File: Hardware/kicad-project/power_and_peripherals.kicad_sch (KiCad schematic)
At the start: 42 parts, among them CN1 Conn_02x08_Odd_Even, CN2 Conn_02x15_Odd_Even, CN3 Conn_02x17_Odd_Even, CN4 Conn_02x10_Odd_Even, J1 Conn_01x02, J2 UART, J3 Torque, J4 Stepper supply, J5 Brake, Q1 Q_NMOS_DGS, Q2 Q_NMOS_DGS, U1 LM7812_TO220, U2 L7805

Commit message: hw: add note to layout and add pdf
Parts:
- renumbered CN3 to CN10, CN4 to CN7, CN1 to CN8, CN2 to CN9
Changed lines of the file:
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@@
   (symbol (lib_id "Connector_Generic:Conn_02x08_Odd_Even") (at 51.308 104.902 0) (unit 1)
     (in_bom yes) (on_board yes) (fields_autoplaced)
-    (property "Reference" "CN1" (id 0) (at 52.578 90.932 0))
-    (property "Value" "Conn_02x08_Odd_Even" (id 1) (at 52.578 93.472 0))
+    (property "Reference" "CN8" (id 0) (at 52.578 90.17 0))
+    (property "Value" "Conn_02x08_Odd_Even" (id 1) (at 52.578 92.71 0))
     (property "Footprint" "Connector_PinHeader_2.54mm:PinHeader_2x08_P2.54mm_Vertical" (id 2) (at 51.308 104.902 0)
       (effects (font (size 1.27 1.27)) hide)
@@
   (symbol (lib_id "Connector_Generic:Conn_02x15_Odd_Even") (at 51.308 146.812 0) (unit 1)
     (in_bom yes) (on_board yes) (fields_autoplaced)
-    (property "Reference" "CN2" (id 0) (at 52.578 122.682 0))
-    (property "Value" "Conn_02x15_Odd_Even" (id 1) (at 52.578 125.222 0))
+    (property "Reference" "CN9" (id 0) (at 52.578 121.92 0))
+    (property "Value" "Conn_02x15_Odd_Even" (id 1) (at 52.578 124.46 0))
     (property "Footprint" "Connector_PinHeader_2.54mm:PinHeader_2x15_P2.54mm_Vertical" (id 2) (at 51.308 146.812 0)
       (effects (font (size 1.27 1.27)) hide)
@@
   (symbol (lib_id "Connector_Generic:Conn_02x17_Odd_Even") (at 99.568 151.892 0) (unit 1)
     (in_bom yes) (on_board yes) (fields_autoplaced)
-    (property "Reference" "CN3" (id 0) (at 100.838 125.222 0))
-    (property "Value" "Conn_02x17_Odd_Even" (id 1) (at 100.838 127.762 0))
+    (property "Reference" "CN10" (id 0) (at 100.838 124.46 0))
+    (property "Value" "Conn_02x17_Odd_Even" (id 1) (at 100.838 127 0))
     (property "Footprint" "Connector_PinHeader_2.54mm:PinHeader_2x17_P2.54mm_Vertical" (id 2) (at 99.568 151.892 0)
       (effects (font (size 1.27 1.27)) hide)
@@
   (symbol (lib_id "Connector_Generic:Conn_02x10_Odd_Even") (at 100.838 107.442 0) (unit 1)
     (in_bom yes) (on_board yes) (fields_autoplaced)
-    (property "Reference" "CN4" (id 0) (at 102.108 90.932 0))
-    (property "Value" "Conn_02x10_Odd_Even" (id 1) (at 102.108 93.472 0))
+    (property "Reference" "CN7" (id 0) (at 102.108 90.17 0))
+    (property "Value" "Conn_02x10_Odd_Even" (id 1) (at 102.108 92.71 0))
     (property "Footprint" "Connector_PinHeader_2.54mm:PinHeader_2x10_P2.54mm_Vertical" (id 2) (at 100.838 107.442 0)
       (effects (font (size 1.27 1.27)) hide)

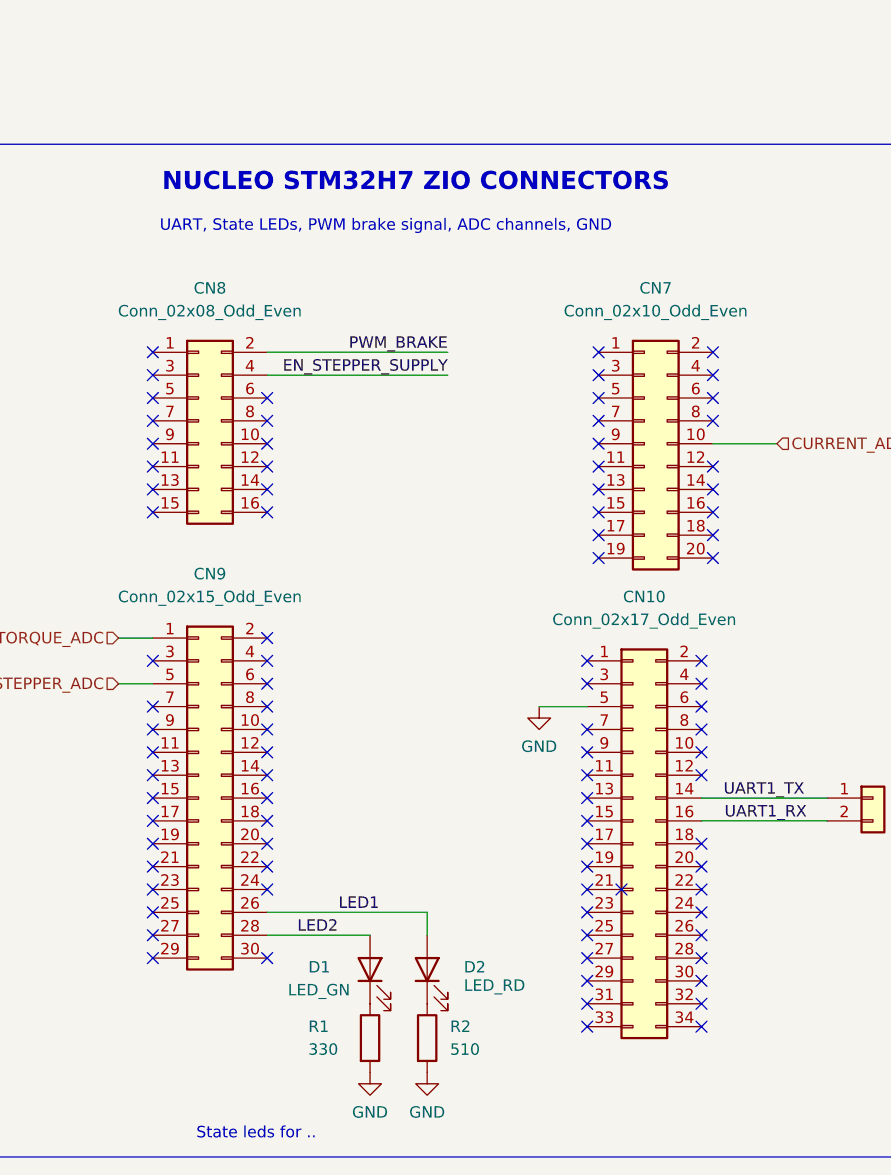
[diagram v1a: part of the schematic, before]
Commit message: hw: add heading to the schematic
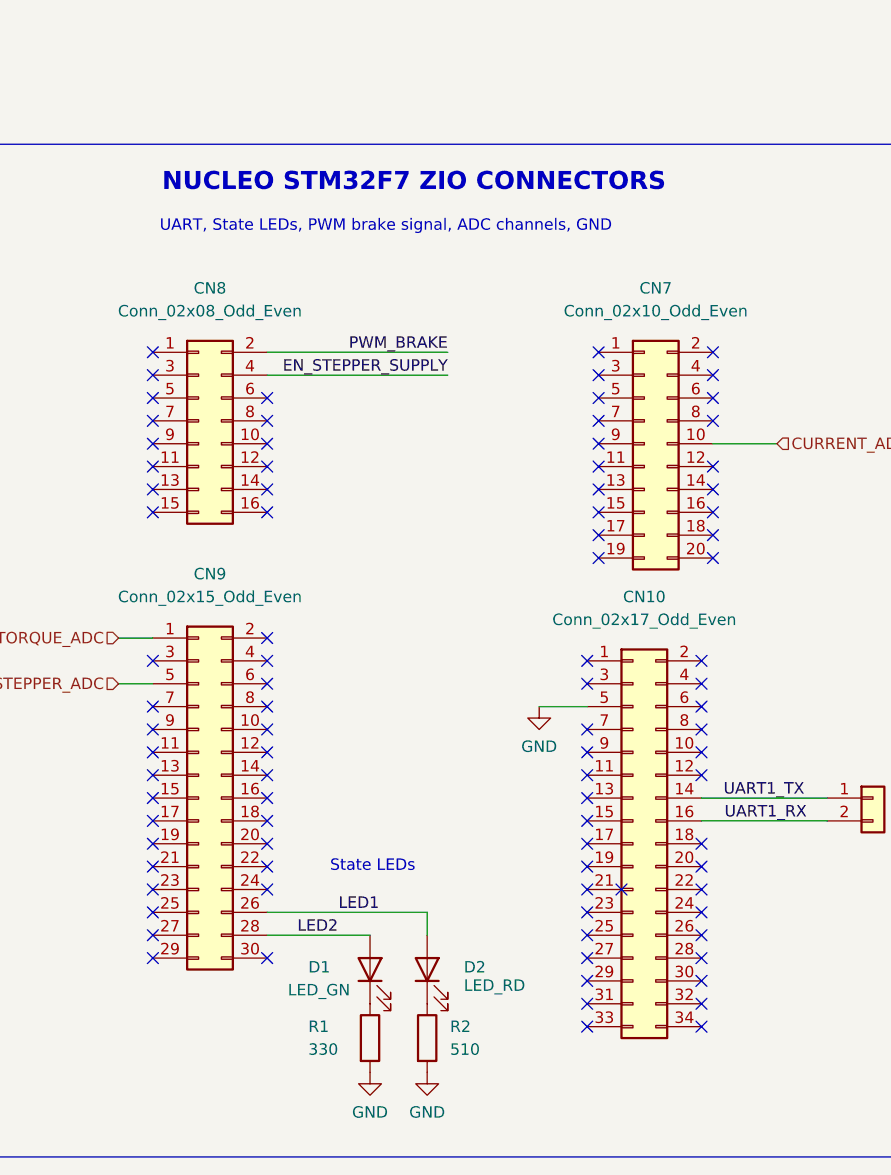
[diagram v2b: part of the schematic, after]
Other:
- note added: "NUCLEO STM32F7 ZIO CONNECTORS"
- note added: "State LEDs"
- note removed: "NUCLEO STM32H7 ZIO CONNECTORS"
- note removed: "State leds for .."
- company: (none) -> ProM Facility 
- title: (none) -> STB - Expansion Board
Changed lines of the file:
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@@
 (kicad_sch (version 20211123) (generator eeschema)
   (paper "A4")
+  (title_block
+    (title "STB - Expansion Board")
+    (date "2022-08-09")
+    (rev "0.2")
+    (company "ProM Facility ")
+  )
   (junction (at 255.27 115.824) (diameter 0) (color 0 0 0 0)
   )
@@
     (effects (font (size 1.27 1.27)) (justify left bottom))
   )
-  (text "NUCLEO STM32H7 ZIO CONNECTORS\n" (at 47.244 79.629 0)
+  (text "NUCLEO STM32F7 ZIO CONNECTORS\n" (at 47.244 79.629 0)
     (effects (font (size 2 2) bold) (justify left bottom))
   )
@@
     (effects (font (size 2 2) (thickness 0.4) bold) (justify left bottom))
   )
-  (text "State leds for .." (at 51.054 184.912 0)
+  (text "State LEDs" (at 65.913 155.194 0)
     (effects (font (size 1.27 1.27)) (justify left bottom))
   )
